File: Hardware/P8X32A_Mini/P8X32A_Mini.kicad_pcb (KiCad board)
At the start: 4 copper layers, 42 x 42 mm, 20 parts, among them J1 Conn_01x09, J2 Conn_01x09, J3 Conn_01x08, J4 Conn_01x08, SW1 SW_PUSH, U1 Propeller, U2 24LC512, Y1 5Mhz

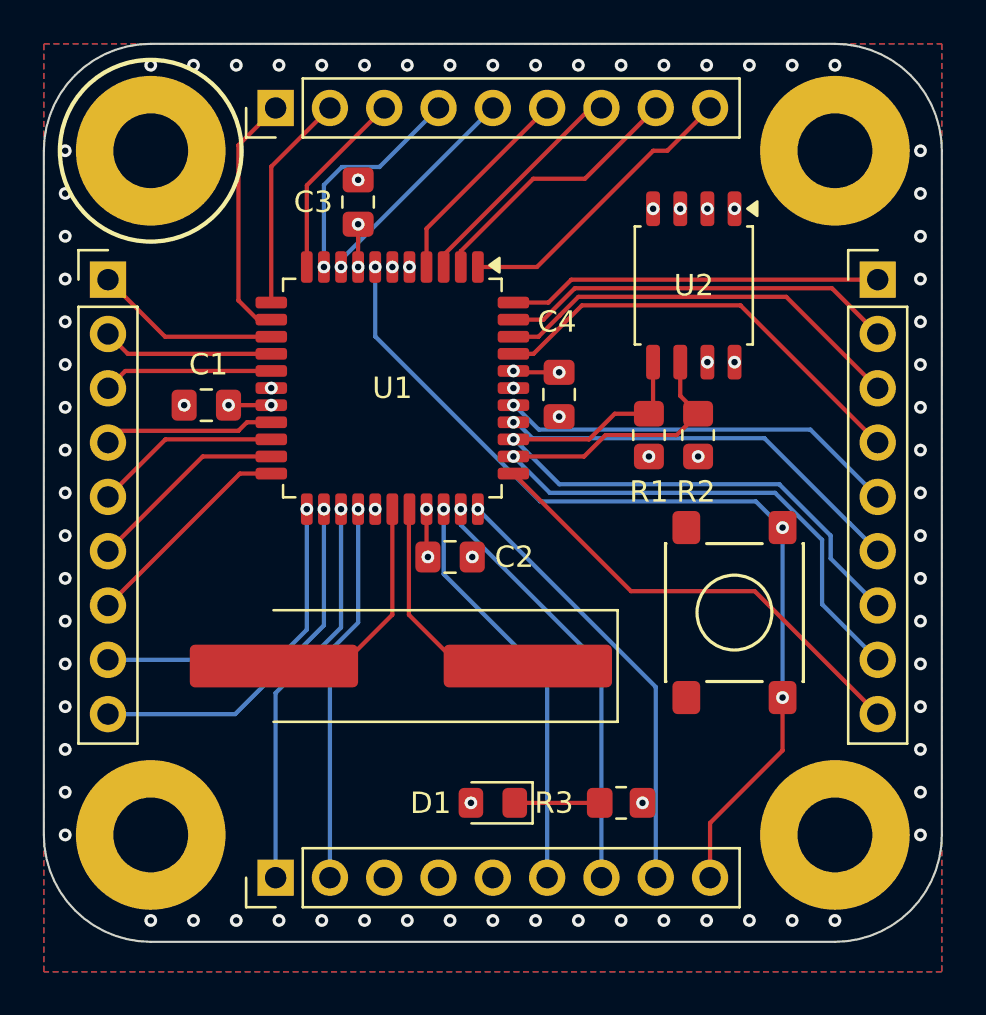
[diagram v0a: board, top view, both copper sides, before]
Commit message: Hardware updates. Add Lr04 lora module datasheets
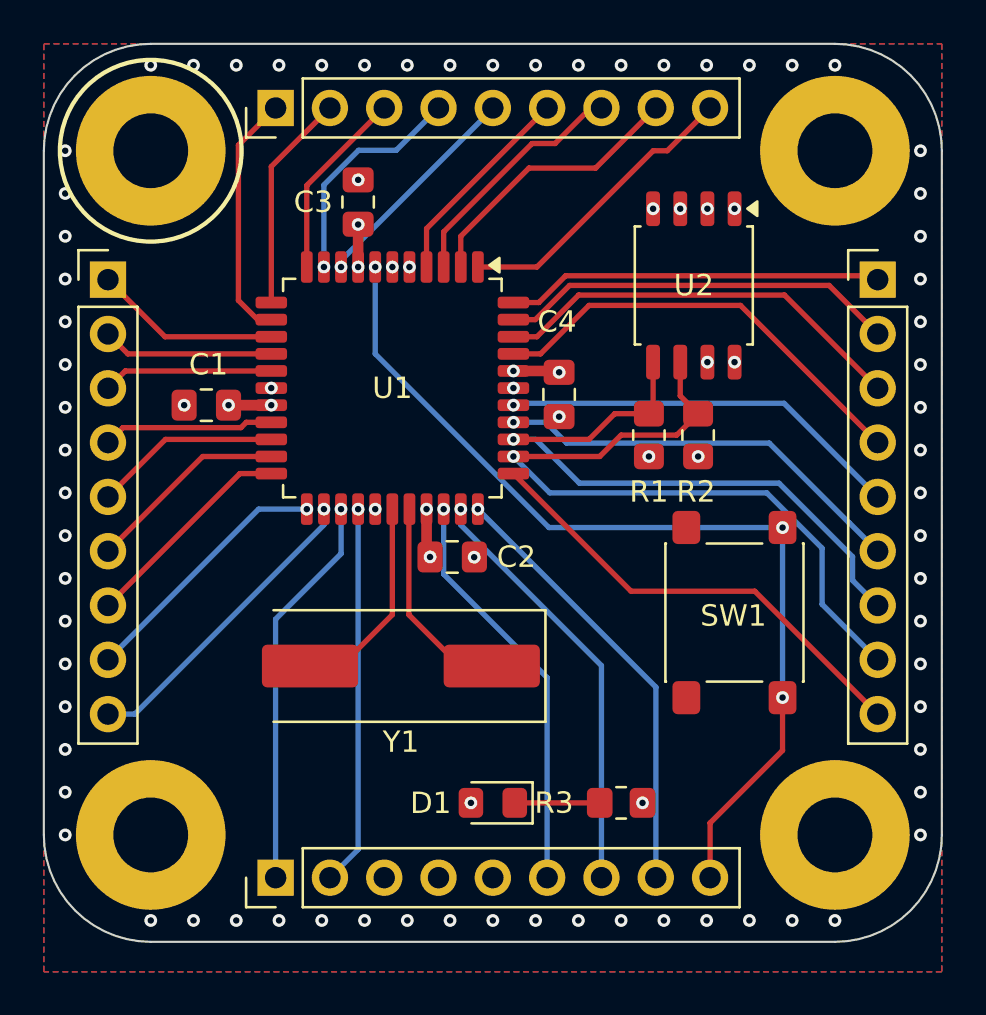
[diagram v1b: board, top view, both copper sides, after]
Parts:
- SW1: footprint General:SW_SPST -> Button_Switch_SMD:SW_SPST_PTS645Sx43SMTR92
- Y1: footprint Crystal:Crystal_SMD_HC49-SD_HandSoldering -> Crystal:Crystal_SMD_HC49-SD
- moved C2 0.10 mm to (142.1, 107.0)
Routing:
- net Net-(U1-XO): track 14.9 -> 11.5 mm
- net P20: track 15.5 -> 12.2 mm
- net P21: track 17.3 -> 14.5 mm
- net P6: track 10.8 -> 11.4 mm
